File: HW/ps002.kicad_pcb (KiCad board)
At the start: 2 copper layers, 20 parts, among them J1 USB, J2 OUT, U1 MC34063

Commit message: PCB Routed
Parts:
- moved C7 8.14 mm to (88.9, 80.0)
- moved C4 7.44 mm to (77.5, 67.3)
- moved C5 7.44 mm to (77.5, 80.0)
- moved C6 6.32 mm to (88.9, 67.3)
- moved L3 5.61 mm to (91.4, 87.6)
- moved C3 4.02 mm to (67.3, 73.7)
- moved J2 2.77 mm to (96.5, 73.7)
- moved L2 2.26 mm to (91.4, 59.7)
- moved D2 1.95 mm to (77.5, 87.6)
- moved D3 1.95 mm to (77.5, 91.4)
- moved C1 1.27 mm to (55.9, 73.7)
- moved J1 1.27 mm to (62.2, 86.4)
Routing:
- net GND: track 2.54 -> 133.6 mm
- net VCC: track 0.00 -> 67.6 mm
- net N-000004: track 0.00 -> 33.6 mm
- net N-0000011: track 0.00 -> 21.2 mm
- net N-0000010: track 0.00 -> 21.2 mm
- net N-000003: track 0.00 -> 17.3 mm
- net N-0000012: track 0.00 -> 15.3 mm
- net N-0000015: track 0.00 -> 15.0 mm
- net N-0000013: track 0.00 -> 12.3 mm
- net N-000002: track 0.00 -> 5.08 mm

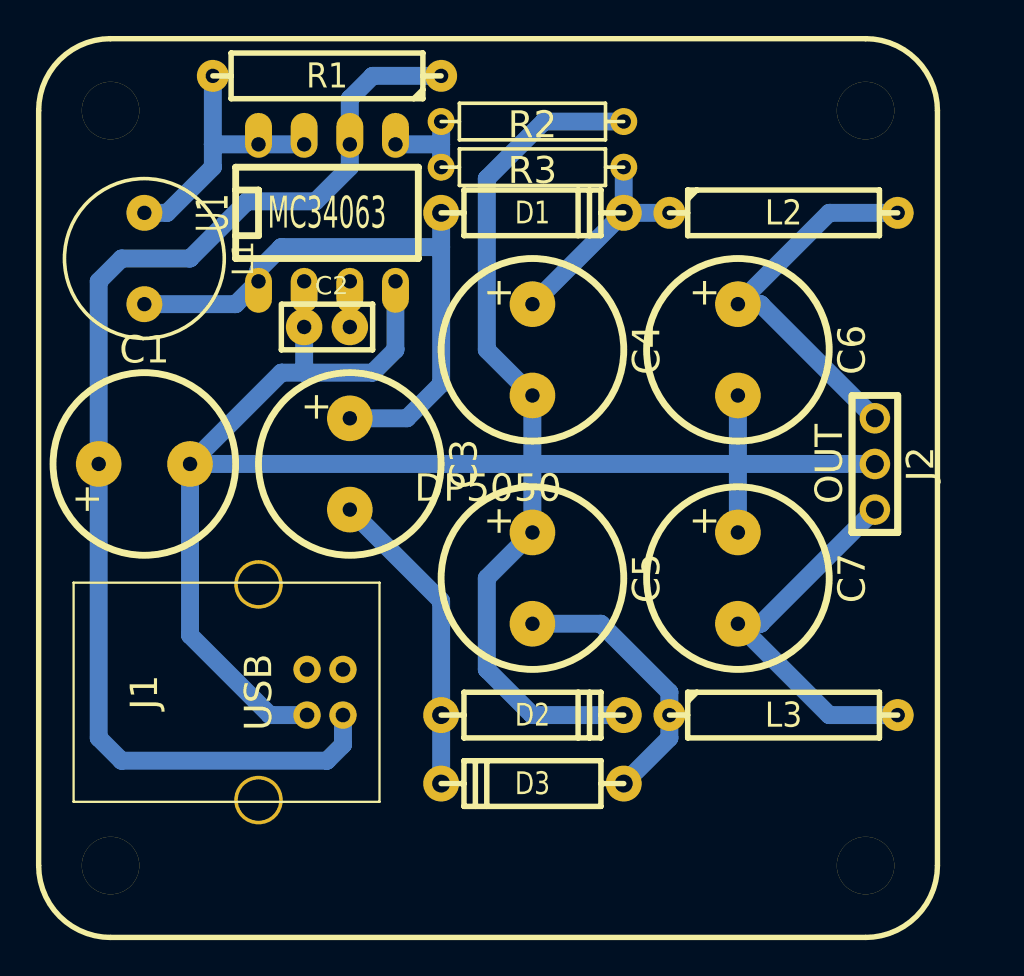
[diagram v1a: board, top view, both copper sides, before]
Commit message: PS002 B version added Separate controllers for positive and negative sides
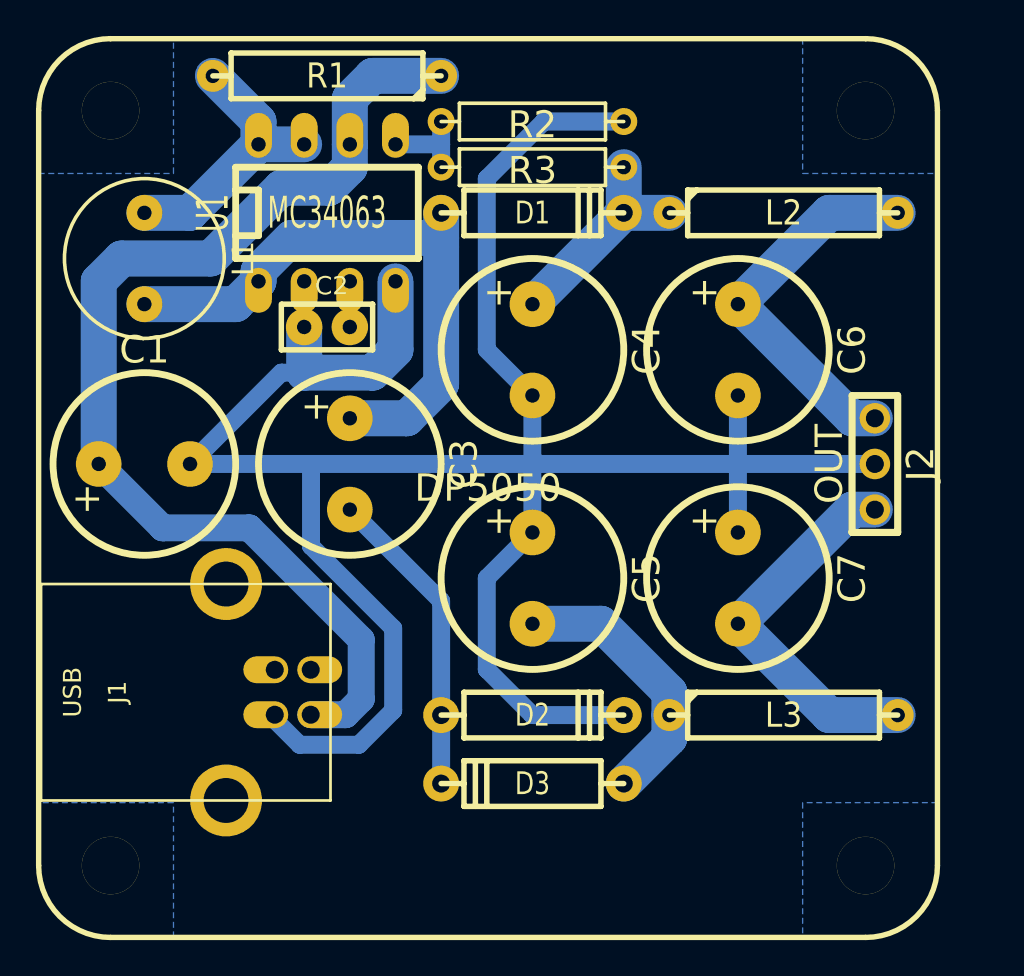
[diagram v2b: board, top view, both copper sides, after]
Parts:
- J1: footprint USB_B -> USB-B
- moved J1 1.91 mm to (64.1, 86.4)
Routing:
- net VCC: track 67.6 -> 61.3 mm
- net GND: track 133.6 -> 139.5 mm
- added copper zone on B.Cu, net GND
